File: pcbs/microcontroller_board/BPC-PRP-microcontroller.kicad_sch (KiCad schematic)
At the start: 21 parts, among them J1 Us_1, J10 Curr_probe, J11 5V, J12 Gnd, J13 I2C, J2 Us_2, J3 Us_3, J4 Line_1, J5 Line_2, J6 Motor_driver_1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

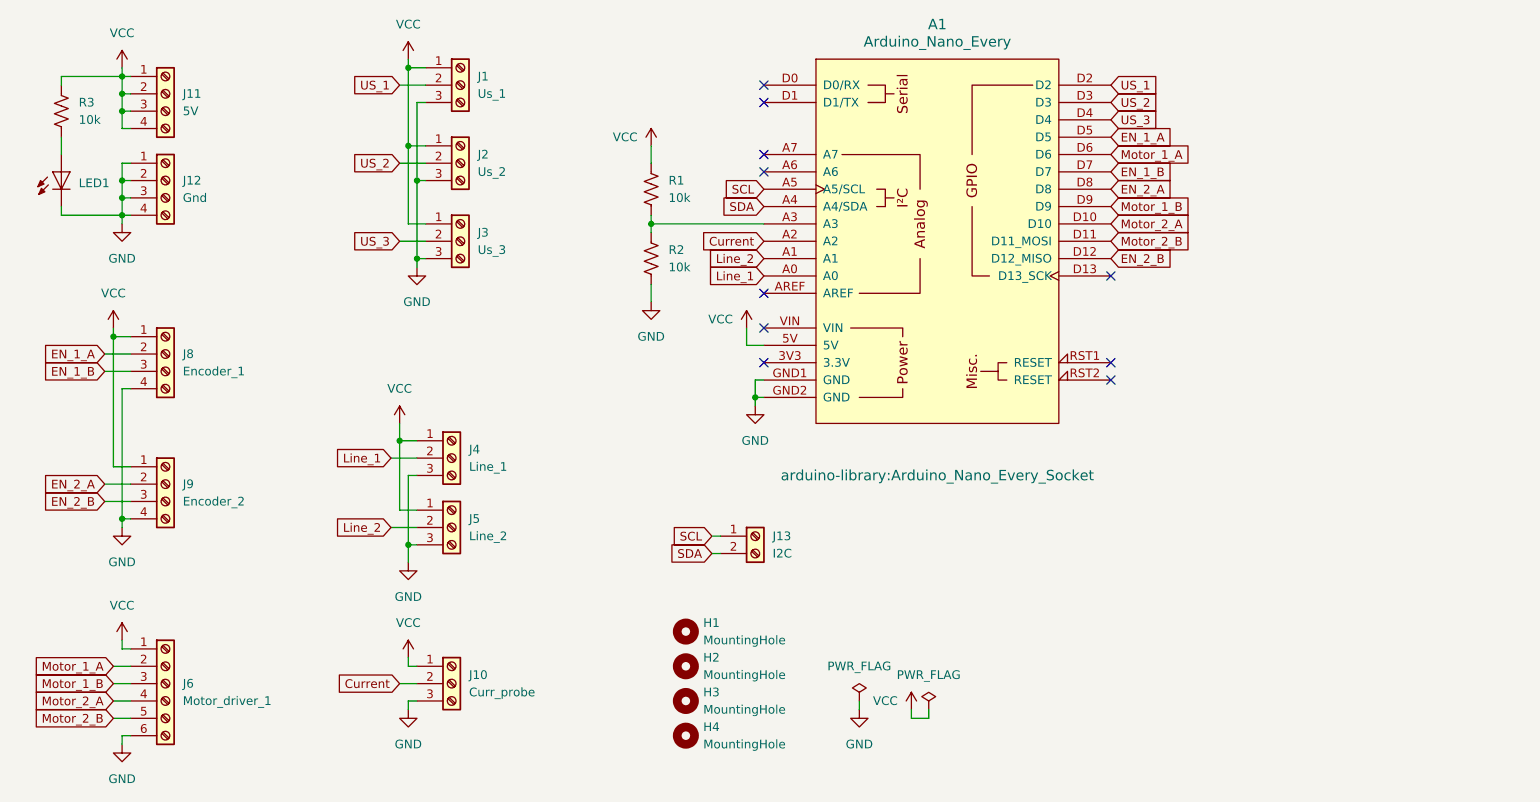
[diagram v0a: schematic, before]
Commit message: updated arduino board, add leds
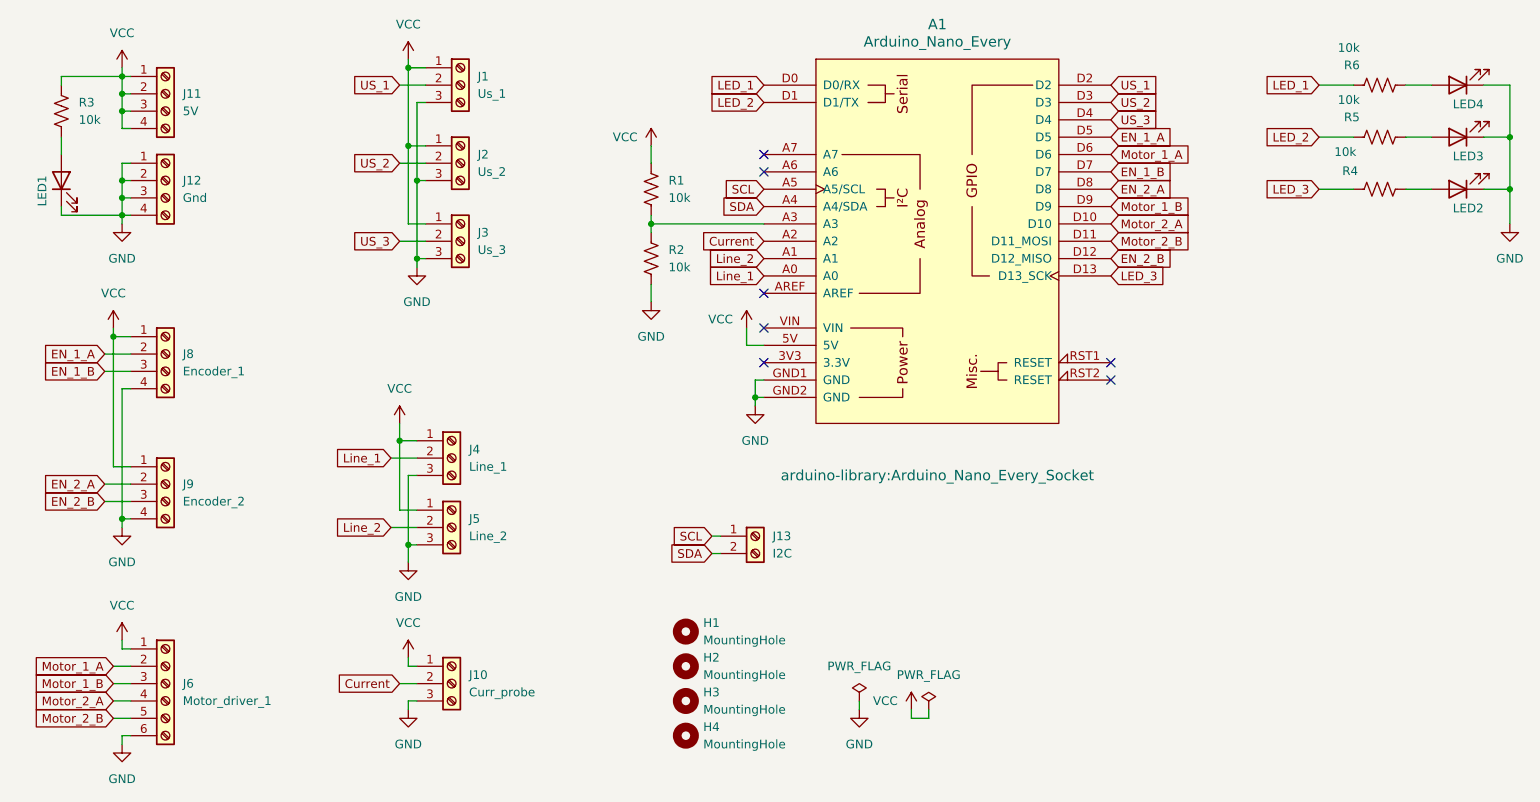
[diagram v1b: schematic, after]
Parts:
- removed LED1: LED, 1206, symbol adafruit:LEDSMT1206
- added LED1, LED2, LED3, LED4: ~, LED_SMD:LED_1206_3216Metric, symbol LED:IR26-21C_L110_TR8
- added R4, R5, R6: 10k, Resistor_SMD:R_1206_3216Metric, symbol Device:R_US
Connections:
- net GND: now also LED1.1 (K), LED2.1 (K), LED3.1 (K), LED4.1 (K)
- net at R3.2: now also LED1.2 (A)
- net LED_1: now reaches A1.D0 (D0/RX)
- net LED_1: now also R6.1
- net LED_2: now reaches A1.D1 (D1/TX)
- net LED_2: now also R5.1
- net LED_3: now reaches A1.D13 (D13_SCK)
- net LED_3: now also R4.1
- new net: LED4.2 (A), R6.2
- new net: LED3.2 (A), R5.2
- new net: LED2.2 (A), R4.2
- no-connect marks 10 -> 7
